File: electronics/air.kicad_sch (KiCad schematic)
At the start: 18 parts, among them J2 Conn_01x10 8.5mm, J3 Conn_01x10 8.5mm, U3 ENS210, U4 LPS22HH, U5 STCC4

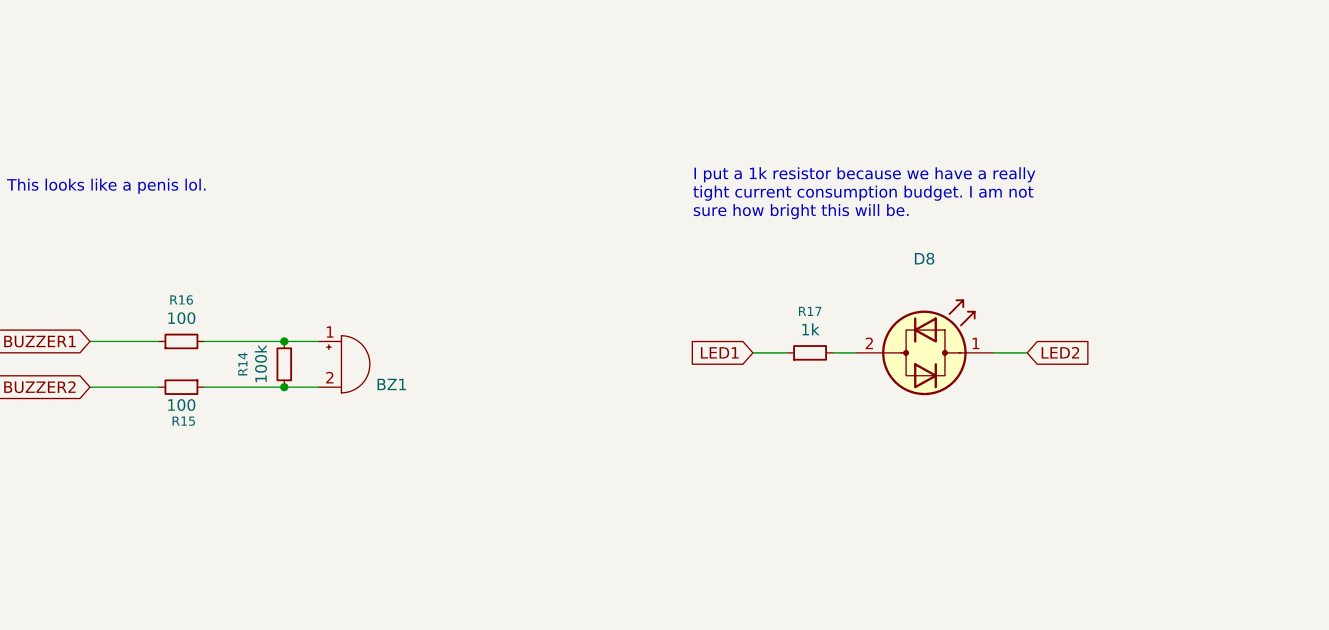
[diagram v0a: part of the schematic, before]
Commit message: Fixed errors of the first hw prototype
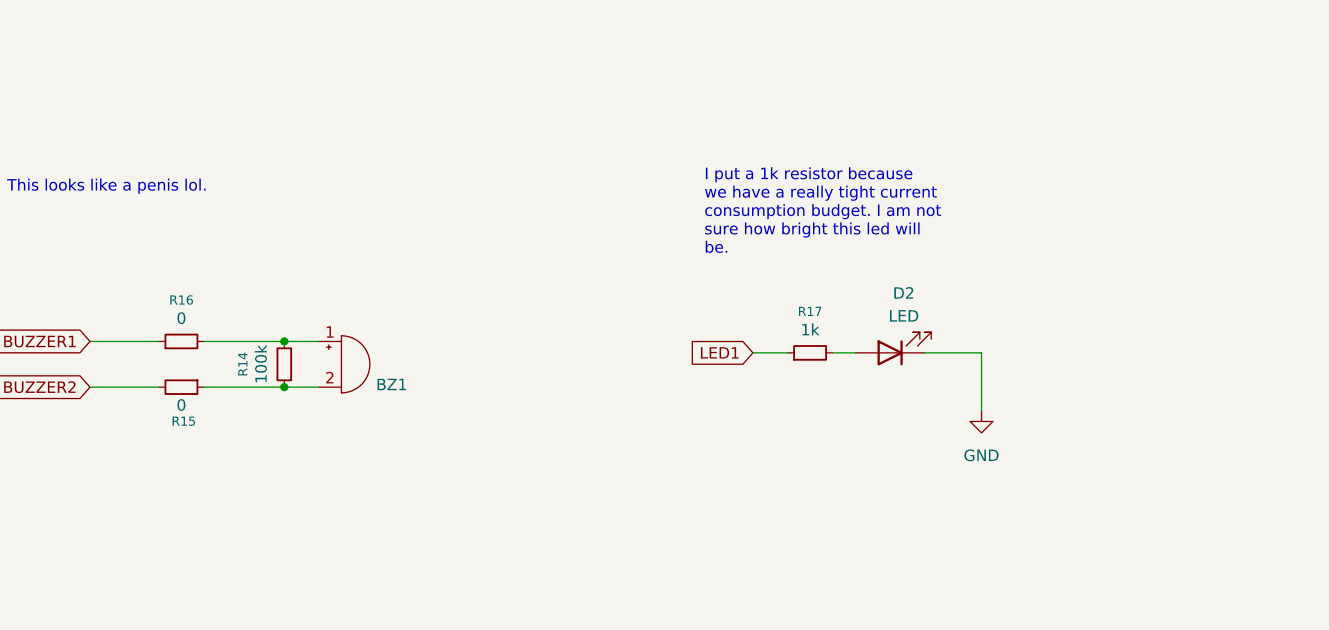
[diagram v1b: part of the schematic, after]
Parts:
- removed D8: ~, LED_SMD:LED_0603_1608Metric_Pad1.05x0.95mm_HandSolder, symbol Device:LED_Dual_Bidirectional
- added D2: LED, LED_SMD:LED_0603_1608Metric_Pad1.05x0.95mm_HandSolder, symbol Device:LED
- R15, R16: value 100 -> 0
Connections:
- net GND: now also D2.1 (K)
- net at R17.2: now also D2.2 (A)
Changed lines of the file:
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@@
 		)
 	)
-	(text_box "I put a 1k resistor because we have a really tight current consumption budget. I am not sure how bright this will be."
+	(text_box "I put a 1k resistor because we have a really tight current consumption budget. I am not sure how bright this led will be."
 		(exclude_from_sim no)
-		(at 196.85 116.84 0)
-		(size 48.26 11.43)
+		(at 198.12 116.84 0)
+		(size 31.75 10.16)
 		(margins 0.9525 0.9525 0.9525 0.9525)
 		(stroke
@@
 	(wire
 		(pts
+			(xy 229.87 138.43) (xy 229.87 144.78)
+		)
+		(stroke
+			(width 0)
+			(type default)
+		)
+	)
+	(wire
+		(pts
 			(xy 72.39 128.27) (xy 81.28 128.27)
 		)
@@
 	(wire
 		(pts
-			(xy 231.14 138.43) (xy 234.95 138.43)
-		)
-		(stroke
-			(width 0)
-			(type default)
-		)
-	)
-	(wire
-		(pts
 			(xy 200.66 46.99) (xy 200.66 41.91)
 		)
@@
 	(wire
 		(pts
+			(xy 223.52 138.43) (xy 229.87 138.43)
+		)
+		(stroke
+			(width 0)
+			(type default)
+		)
+	)
+	(wire
+		(pts
 			(xy 74.93 171.45) (xy 74.93 176.53)
 		)
@@
 		)
 	)
-	(global_label "LED2"
-		(shape input)
-		(at 234.95 138.43 0)
-		(fields_autoplaced yes)
-		(effects
-			(font
-				(size 1.27 1.27)
-			)
-			(justify left)
-		)
-		(property "Intersheetrefs" "${INTERSHEET_REFS}"
-			(at 242.5918 138.43 0)
-			(effects
-				(font
-					(size 1.27 1.27)
-				)
-				(justify left)
-				(hide yes)
-			)
-		)
-	)
 	(global_label "CAP3.1"
 		(shape input)
@@
 	)
 	(symbol
+		(lib_id "power:GND")
+		(at 229.87 144.78 0)
+		(unit 1)
+		(exclude_from_sim no)
+		(in_bom yes)
+		(on_board yes)
+		(dnp no)
+		(fields_autoplaced yes)
+		(property "Reference" "#PWR017"
+			(at 229.87 151.13 0)
+			(effects
+				(font
+					(size 1.27 1.27)
+				)
+				(hide yes)
+			)
+		)
+		(property "Value" "GND"
+			(at 229.87 149.86 0)
+			(effects
+				(font
+					(size 1.27 1.27)
+				)
+			)
+		)
+		(property "Footprint" ""
+			(at 229.87 144.78 0)
+			(effects
+				(font
+					(size 1.27 1.27)
+				)
+				(hide yes)
+			)
+		)
+		(property "Datasheet" ""
+			(at 229.87 144.78 0)
+			(effects
+				(font
+					(size 1.27 1.27)
+				)
+				(hide yes)
+			)
+		)
+		(property "Description" "Power symbol creates a global label with name \"GND\" , ground"
+			(at 229.87 144.78 0)
+			(effects
+				(font
+					(size 1.27 1.27)
+				)
+				(hide yes)
+			)
+		)
+		(pin "1"
+		)
+		(instances
+			(project ""
+				(path "/52e127d5-d526-426f-bc25-1382db54c478/22aa362c-b9a5-4bc8-a884-49007f36f5e7"
+					(reference "#PWR017")
+					(unit 1)
+				)
+			)
+		)
+	)
+	(symbol
 		(lib_id "Connector_Generic:Conn_01x10")
 		(at 85.09 163.83 0)
@@
 	)
 	(symbol
-		(lib_id "Device:LED_Dual_Bidirectional")
-		(at 223.52 138.43 0)
-		(unit 1)
-		(exclude_from_sim no)
-		(in_bom yes)
-		(on_board yes)
-		(dnp no)
-		(property "Reference" "D8"
-			(at 223.52 128.016 0)
-			(effects
-				(font
-					(size 1.27 1.27)
-				)
-			)
-		)
-		(property "Value" "~"
-			(at 223.52 130.556 0)
-			(effects
-				(font
-					(size 1.27 1.27)
-				)
-			)
-		)
-		(property "Footprint" "LED_SMD:LED_0603_1608Metric_Pad1.05x0.95mm_HandSolder"
-			(at 223.52 138.43 0)
-			(effects
-				(font
-					(size 1.27 1.27)
-				)
-				(hide yes)
-			)
-		)
-		(property "Datasheet" "~"
-			(at 223.52 138.43 0)
-			(effects
-				(font
-					(size 1.27 1.27)
-				)
-				(hide yes)
-			)
-		)
-		(property "Description" "Dual LED, bidirectional"
-			(at 223.52 138.43 0)
-			(effects
-				(font
-					(size 1.27 1.27)
-				)
-				(hide yes)
-			)
-		)
-		(pin "2"
-		)
-		(pin "1"
-		)
-		(instances
-			(project ""
-				(path "/52e127d5-d526-426f-bc25-1382db54c478/22aa362c-b9a5-4bc8-a884-49007f36f5e7"
-					(reference "D8")
-					(unit 1)
-				)
-			)
-		)
-	)
-	(symbol
 		(lib_id "Connector_Generic:Conn_01x10")
 		(at 86.36 128.27 0)
@@
 			)
 		)
-		(property "Value" "100"
+		(property "Value" "0"
 			(at 140.97 144.272 90)
 			(effects
@@
 	)
 	(symbol
+		(lib_id "Device:LED")
+		(at 219.71 138.43 180)
+		(unit 1)
+		(exclude_from_sim no)
+		(in_bom yes)
+		(on_board yes)
+		(dnp no)
+		(property "Reference" "D2"
+			(at 221.234 131.826 0)
+			(effects
+				(font
+					(size 1.27 1.27)
+				)
+			)
+		)
+		(property "Value" "LED"
+			(at 221.234 134.366 0)
+			(effects
+				(font
+					(size 1.27 1.27)
+				)
+			)
+		)
+		(property "Footprint" "LED_SMD:LED_0603_1608Metric_Pad1.05x0.95mm_HandSolder"
+			(at 219.71 138.43 0)
+			(effects
+				(font
+					(size 1.27 1.27)
+				)
+				(hide yes)
+			)
+		)
+		(property "Datasheet" "~"
+			(at 219.71 138.43 0)
+			(effects
+				(font
+					(size 1.27 1.27)
+				)
+				(hide yes)
+			)
+		)
+		(property "Description" "Light emitting diode"
+			(at 219.71 138.43 0)
+			(effects
+				(font
+					(size 1.27 1.27)
+				)
+				(hide yes)
+			)
+		)
+		(property "Sim.Pins" "1=K 2=A"
+			(at 219.71 138.43 0)
+			(effects
+				(font
+					(size 1.27 1.27)
+				)
+				(hide yes)
+			)
+		)
+		(pin "1"
+		)
+		(pin "2"
+		)
+		(instances
+			(project ""
+				(path "/52e127d5-d526-426f-bc25-1382db54c478/22aa362c-b9a5-4bc8-a884-49007f36f5e7"
+					(reference "D2")
+					(unit 1)
+				)
+			)
+		)
+	)
+	(symbol
 		(lib_id "Device:R_Small")
 		(at 140.97 137.16 90)
@@
 			)
 		)
-		(property "Value" "100"
+		(property "Value" "0"
 			(at 140.97 134.62 90)
 			(effects
